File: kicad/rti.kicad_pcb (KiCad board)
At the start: 2 copper layers, 100 x 80 mm, 58 parts, among them J1 Phoenix MKDS, J10 Header 2x3, J11 JST PH 4, J2 NRJ6HF, J3 NRJ6HF, J4 MEBP 8-8G, J5 MEBP 8-8G, J6 JST PH 3, J7 JST PH 3, J8 JST PH 3, J9 JST PH 3, M3 MountingHole_3.2mm_M3_DIN965, M3_2 MountingHole_3.2mm_M3_DIN965, M3_3 MountingHole_3.2mm_M3_DIN965, Q1 BD140, Q10 BD140, Q11 BD140, Q12 BD140, Q13 BD140, Q14 BD140, Q15 BD140, Q16 BD140, Q2 BD140, Q3 BD140, Q4 BD140, Q5 BD140, Q6 BD140, Q7 BD140, Q8 BD140, Q9 BD140, SW1 Switch, SW2 Switch, U1 ATMEGA328-PU, U2 TPIC6B595N, U3 TPIC6B595N, U4 PC827, U5 LM317T, U6 L7805CV, Y1 16MHz

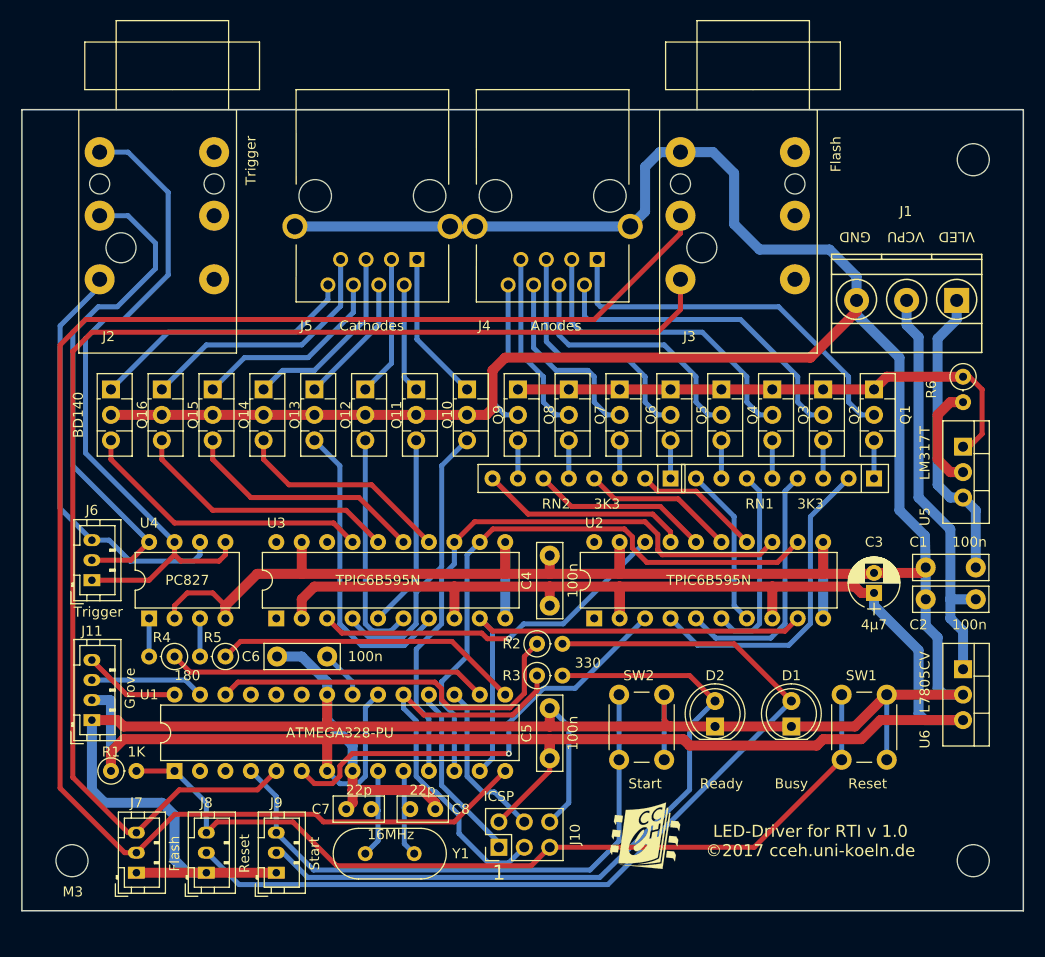
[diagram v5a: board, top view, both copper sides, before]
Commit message: Change LED connectors pinout
Implements a less spectacular failure mode if LED connectors
are switched, ie. flashes them in the wrong order instead of
burning them all.
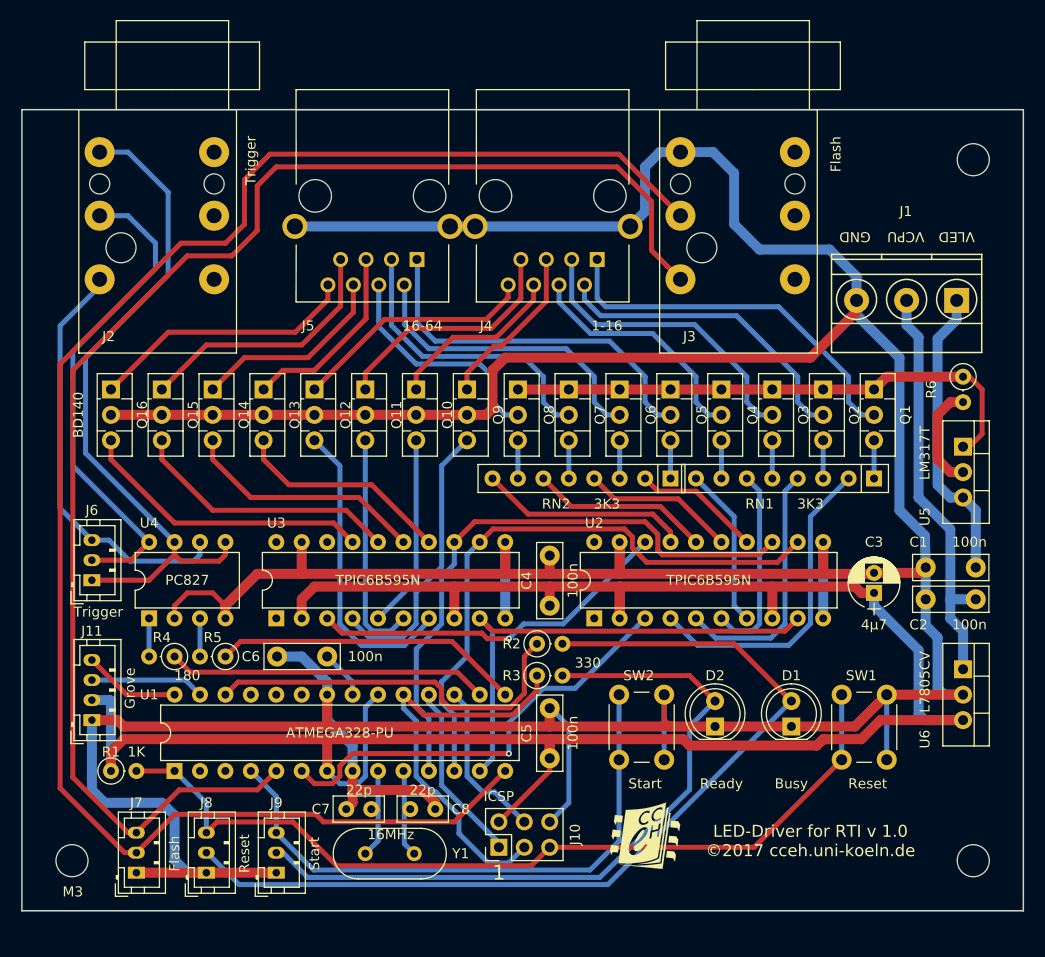
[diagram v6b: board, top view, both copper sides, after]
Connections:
- J4 pad 5: /An4 -> /Cat0
- J4 pad 6: /An5 -> /Cat1
- J4 pad 7: /An6 -> /Cat2
- J4 pad 8: /An7 -> /Cat3
- J5 pad 1: /Cat0 -> /An4
- J5 pad 2: /Cat1 -> /An5
- J5 pad 3: /Cat2 -> /An6
- J5 pad 4: /Cat3 -> /An7
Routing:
- net /An4: track 25.1 -> 36.9 mm
- net /D3: track 133.7 -> 145.2 mm
- net /An5: track 19.1 -> 30.6 mm
- net /Cat3: track 13.1 -> 24.4 mm
- net /An6: track 18.2 -> 29.5 mm
- net /Cat2: track 14.1 -> 24.2 mm
- net /An7: track 15.4 -> 23.2 mm
- net /Cat1: track 10.9 -> 17.8 mm
- net /D8: track 163.8 -> 169.3 mm
- net /An3: track 26.0 -> 24.1 mm
- net /Cat0: track 15.1 -> 16.7 mm
- net /An2: track 31.6 -> 30.4 mm
- net Net-(J2-Pad3): track 69.7 -> 68.6 mm
- net Net-(J2-Pad2): track 50.7 -> 49.6 mm
- net /An1: track 32.5 -> 31.6 mm
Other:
- board text added: "1-16"
- board text added: "16-64"
- board text removed: "Anodes"
- board text removed: "Cathodes"

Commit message: Update kicad format
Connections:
- net /~RESET renamed /~{RESET}
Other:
- net class +5V removed
- net class Default removed
- net class HC removed
- net class HC2HC removed
